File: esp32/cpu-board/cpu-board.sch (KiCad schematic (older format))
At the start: 69 parts, among them J1 Conn_01x06, J2 Conn_01x08, J3 Conn_01x10, J4 Conn_01x10, J5 Conn_01x06, Q1 IRLI640G, Q2 PMBTA42DS,125, Q3 PMBTA42DS,125, Q4 PMBTA42DS,125, Q5 PMBTA42DS,125, Q6 PMBTA42DS,125, U1 ESP32-DevBoard2, U2 MAX7320, U3 MAX7320, U4 MAX7320, U5 V7803-1000, U6 MAX1771

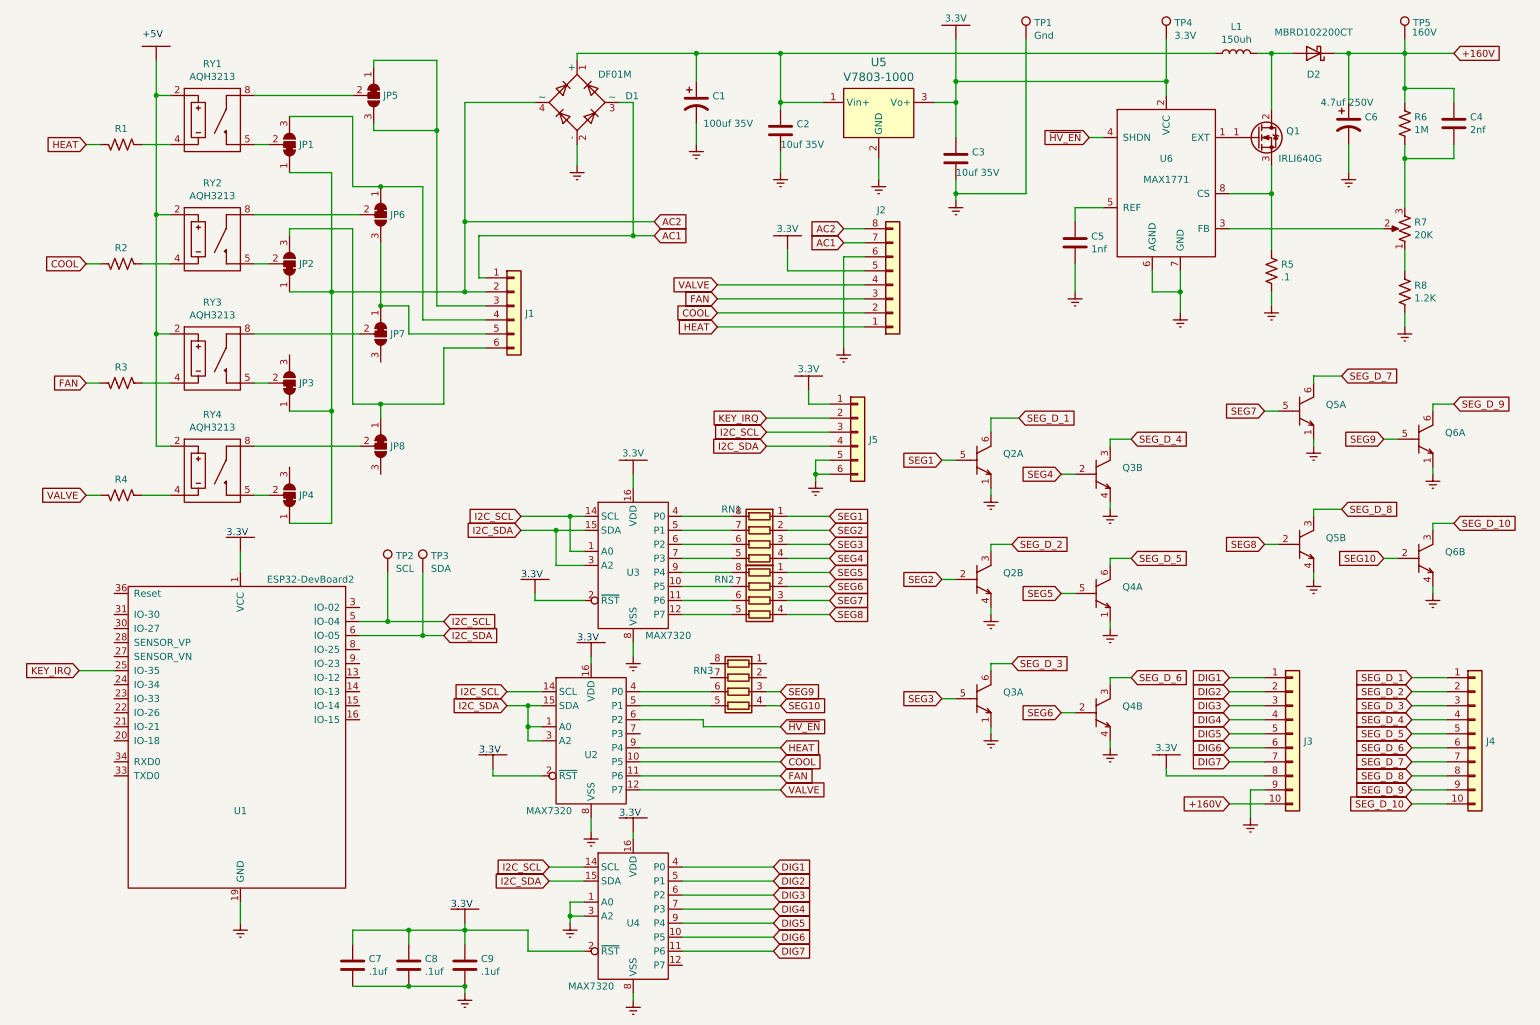
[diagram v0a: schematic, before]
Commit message: Added ground connection, broke the schematic into two sheets
[git-p4: depot-paths = "//depot/nixiestat/": change = 316]
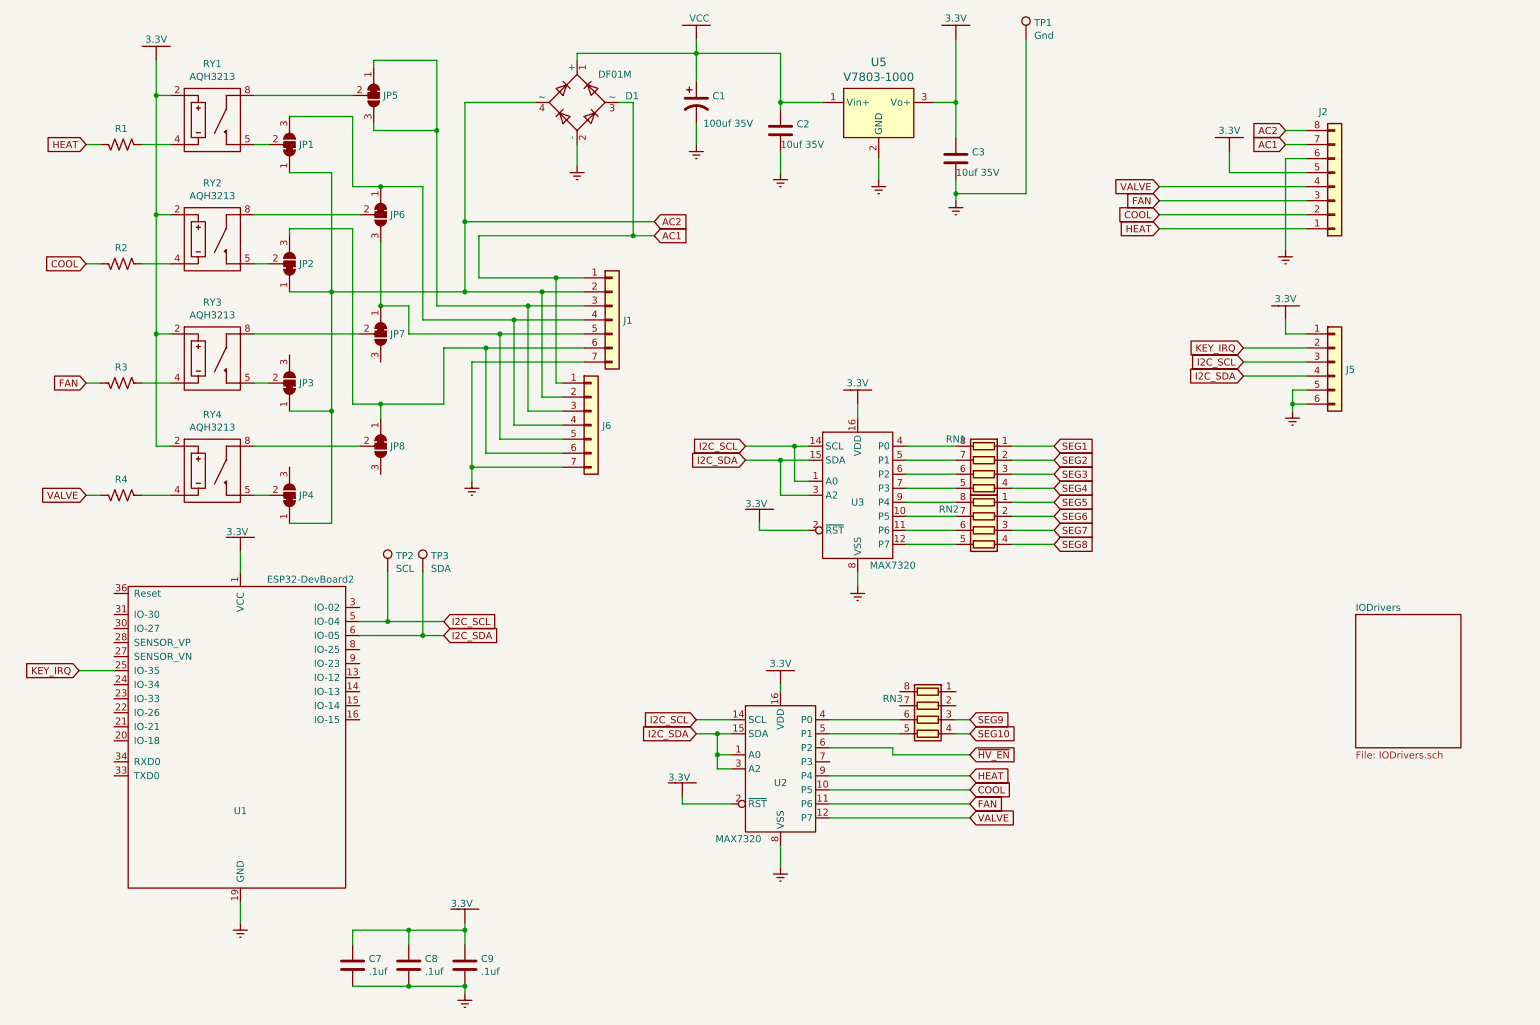
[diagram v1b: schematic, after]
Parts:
- removed C4: 2nf, Resistor_SMD:R_0805_2012Metric_Pad1.20x1.40mm_HandSolder, symbol Device:C
- removed C5: 1nf, Capacitor_SMD:C_0805_2012Metric_Pad1.18x1.45mm_HandSolder, symbol Device:C
- removed C6: 4.7uf 250V, Capacitor_THT:CP_Radial_D6.3mm_P2.50mm, symbol Device:CP1
- removed D2: MBRD102200CT, Diode_SMD:D_SMB, symbol Device:D_Schottky
- removed J1: Conn_01x06, croftj:TES-1-2834015-6, symbol Connector_Generic:Conn_01x06
- removed J3, J4: Conn_01x10, croftj:Mill-Max-295x10, symbol Connector_Generic:Conn_01x10
- removed L1: 150uh, Inductor_SMD:L_12x12mm_H8mm, symbol Device:L
- removed Q1: IRLI640G, Package_TO_SOT_THT:TO-220-3_Vertical, symbol Transistor_FET:IRLIZ44N
- removed Q2, Q3, Q4, Q5, Q6: PMBTA42DS,125, Package_TO_SOT_SMD:SuperSOT-6, symbol croftj:PBMTA42-Dual_NPN_E_1
- removed R5: .1, Resistor_SMD:R_0805_2012Metric_Pad1.20x1.40mm_HandSolder, symbol Device:R_US
- removed R6: 1M, Resistor_SMD:R_0805_2012Metric_Pad1.20x1.40mm_HandSolder, symbol Device:R_US
- removed R7: 20K, Potentiometer_THT:Potentiometer_Bourns_3296W_Vertical, symbol Device:R_POT_US
- removed R8: 1.2K, Resistor_SMD:R_0805_2012Metric_Pad1.20x1.40mm_HandSolder, symbol Device:R_US
- removed TP4: 3.3V, Connector_Pin:Pin_D1.3mm_L11.0mm, symbol Connector:TestPoint
- removed TP5: 160V, Connector_Pin:Pin_D1.3mm_L11.0mm, symbol Connector:TestPoint
- removed U4: MAX7320, Package_SO:TSSOP-16_4.4x5mm_P0.65mm, symbol croftj:MAX7320
- removed U6: MAX1771, Package_SO:SO-8_3.9x4.9mm_P1.27mm, symbol croftj:MAX1771
- removed V11, V8: 3.3V, symbol croftj:3.3V
- added J1: Conn_01x07, croftj:conn-phx-1703090, symbol Connector_Generic:Conn_01x07
- added J6: Conn_01x07, croftj:Mill-Max-295x7, symbol Connector_Generic:Conn_01x07
- added V?: VCC, symbol croftj:VCC
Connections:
- net AC1: now also J1.1 (Pin_1), J6.1 (Pin_1)
- net AC2: now also J1.2 (Pin_2), J6.2 (Pin_2)
- net GNDREF: now also J1.7 (Pin_7), J6.7 (Pin_7)
- net VCC: now reaches C1.1, C2.1, D1.1 (+), U5.1 (Vin+)
- net VCC: now also V?.1 (VCC)
- net at JP1.3 (B), JP6.1 (A): now also J1.4 (Pin_4), J6.4 (Pin_4)
- net at JP2.3 (B), JP8.1 (A): now also J1.6 (Pin_6), J6.6 (Pin_6)
- net at JP5.1 (A), JP5.3 (B): now also J1.3 (Pin_3), J6.3 (Pin_3)
- net at JP6.3 (B), JP7.1 (A): now also J1.5 (Pin_5), J6.5 (Pin_5)
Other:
- note removed: "+5V"
- moved on the sheet: J2, J5, RN1, RN2, RN3, U2, U3

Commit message: First attempt at ensuring proper grounding Added capacitor to the reset pin Extended the reset line to the IO extenders
[git-p4: depot-paths = "//depot/nixiestat/": change = 324]
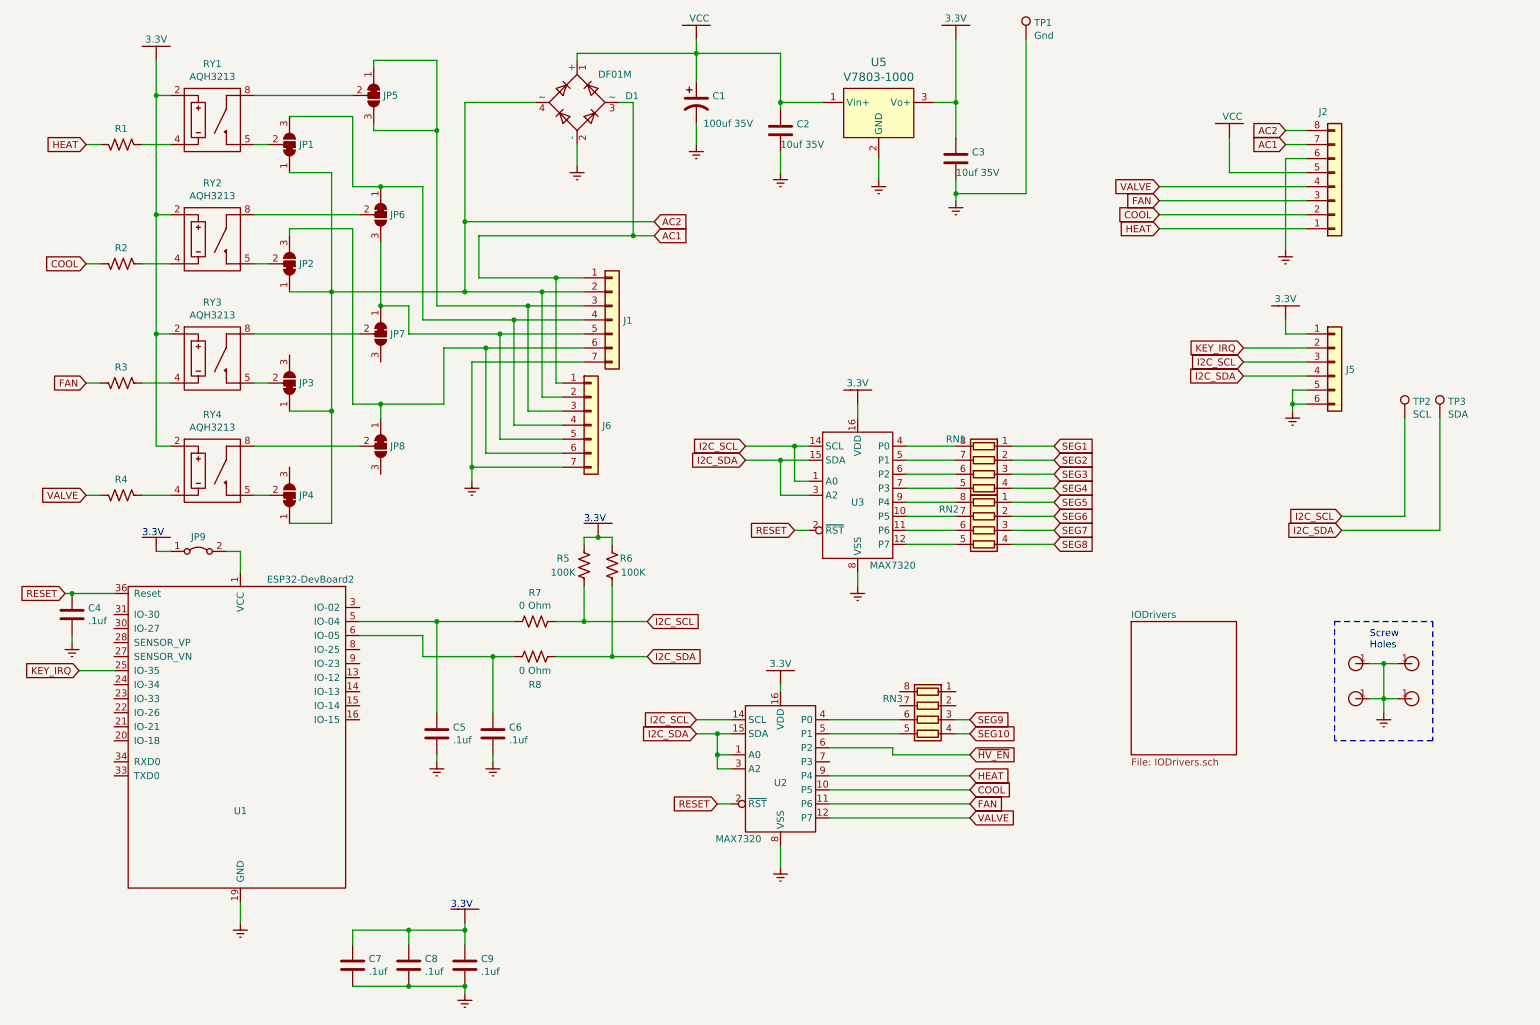
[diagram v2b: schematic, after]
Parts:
- removed V4, V9: 3.3V, symbol croftj:3.3V
- added C4, C5, C6: .1uf, Capacitor_SMD:C_0805_2012Metric_Pad1.18x1.45mm_HandSolder, symbol Device:C
- added JP9: Jumper_2_Bridged, Jumper:SolderJumper-2_P1.3mm_Bridged_RoundedPad1.0x1.5mm, symbol Jumper:Jumper_2_Bridged
- added R5, R6: 100K, Resistor_SMD:R_0805_2012Metric_Pad1.20x1.40mm_HandSolder, symbol Device:R_US
- added R7, R8: 0 Ohm, Resistor_SMD:R_0805_2012Metric_Pad1.20x1.40mm_HandSolder, symbol Device:R_US
- added SH1, SH2, SH3, SH4: ScrewHole, croftj:4-40-Screw, symbol croftj:ScrewHole
- added V8: VCC, symbol croftj:VCC
- gave numbers to parts that had none: 1
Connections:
- net +3.3V: now also JP9.1 (A), R5.1, R6.1; no longer J2.5 (Pin_5), U1.1 (VCC), U2.2 (~RST~), U3.2 (~RST~)
- net GNDREF: now also C4.2, C5.2, C6.2, SH1.1, SH2.1, SH3.1, SH4.1
- net I2C_SCL: now also R5.2, R7.1; no longer U1.5 (IO-04)
- net I2C_SDA: now also R6.2, R8.1; no longer U1.6 (IO-05)
- net VCC: now also J2.5 (Pin_5), V8.1 (VCC)
- net RESET: now reaches U1.36 (Reset)
- net RESET: now also U2.2 (~RST~), U3.2 (~RST~), C4.1
- new net: JP9.2 (B), U1.1 (VCC)
- new net: C5.1, R7.2, U1.5 (IO-04)
- new net: C6.1, R8.2, U1.6 (IO-05)
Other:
- note added: "Screw\nHoles"
- moved on the sheet: TP2, TP3

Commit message: Added RTC
[git-p4: depot-paths = "//depot/nixiestat/": change = 335]
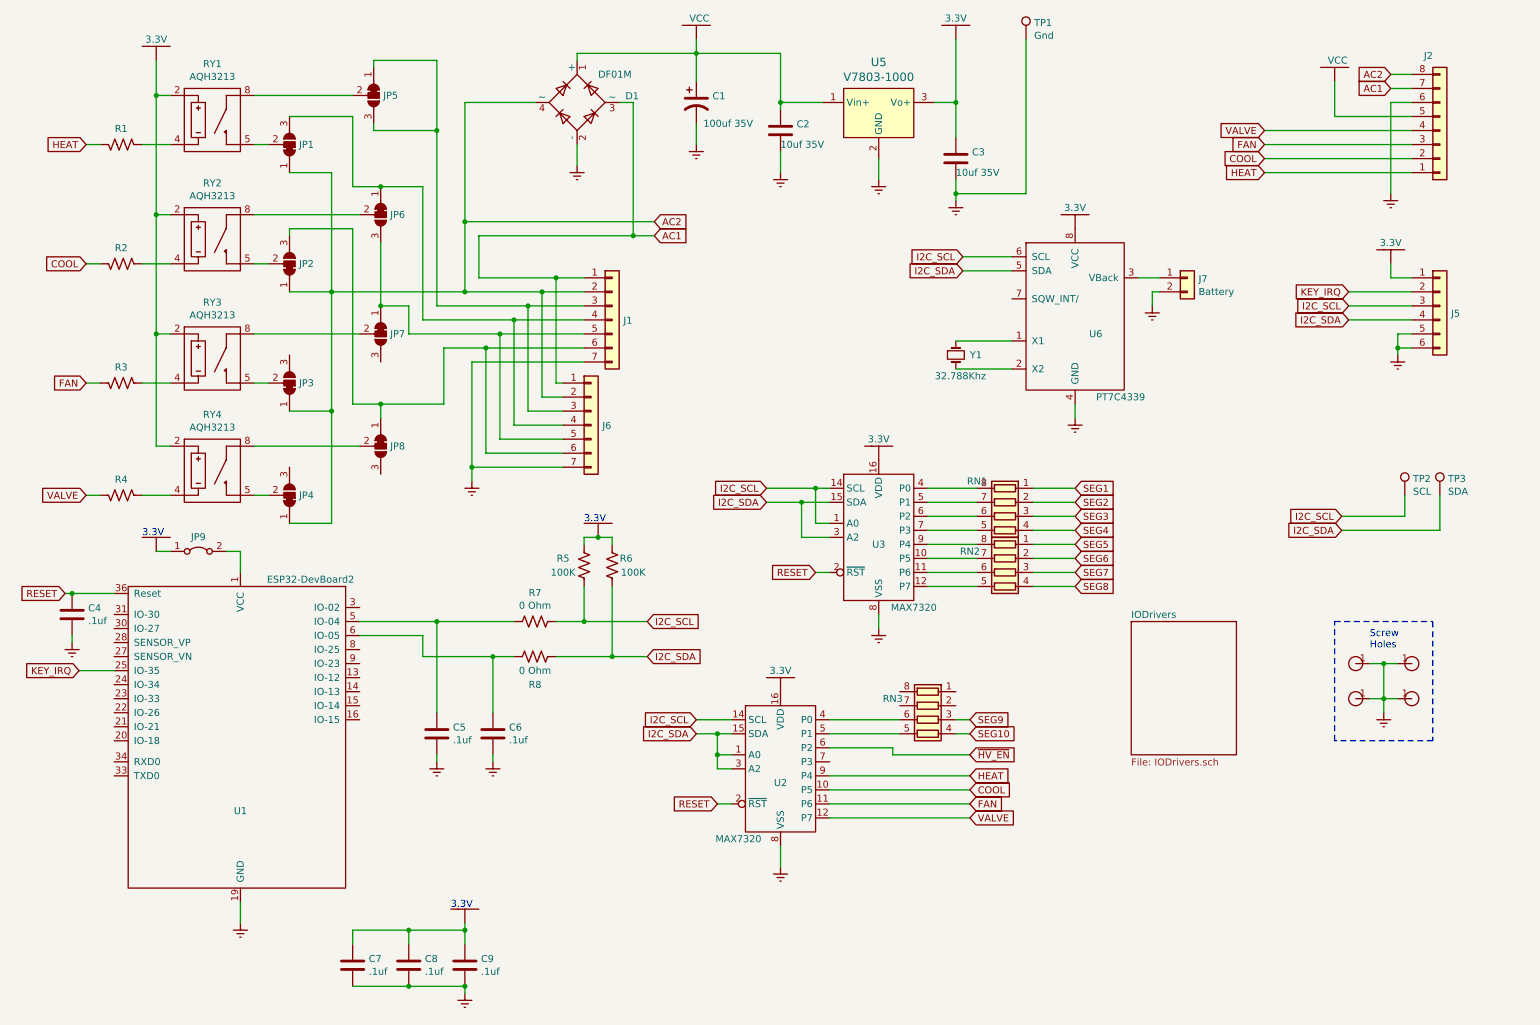
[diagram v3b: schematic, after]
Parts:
- added J7: Battery, Connector_PinHeader_2.54mm:PinHeader_1x02_P2.54mm_Vertical, symbol Connector_Generic:Conn_01x02
- added U6: PT7C4339, Package_SO:SOIC-8_3.9x4.9mm_P1.27mm, symbol croftj:PT7C4339
- added V9: 3.3V, symbol croftj:3.3V
- added Y1: 32.788Khz, Crystal:Crystal_SMD_G8-2Pin_3.2x1.5mm_HandSoldering, symbol Device:Crystal_Small
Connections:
- net +3.3V: now also U6.8 (VCC), V9.1 (+3.3V)
- net GNDREF: now also J7.2 (Pin_2), U6.4 (GND)
- net I2C_SCL: now also U6.6 (SCL)
- net I2C_SDA: now also U6.5 (SDA)
- new net: U6.1 (X1), Y1.1
- new net: U6.2 (X2), Y1.2
- new net: J7.1 (Pin_1), U6.3 (VBack)
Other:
- moved on the sheet: J2, J5, RN1, RN2, TP2, TP3, U3
